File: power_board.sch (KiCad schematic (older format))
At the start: 24 parts

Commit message: Added to the list of parts and started putting parameters on parts in the schematic
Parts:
- removed Q? (x11): Q_NMOS_DGS, symbol Q_NMOS_DGS
- removed Q? (x11): Q_PMOS_DGS, symbol Q_PMOS_DGS
- added D?: LED_CRGB, symbol LED_CRGB
- added R?: R, Resistors_SMD:R_0402, symbol R
- Q?: Continuous Current (none) -> 200mA; Drive Voltage (none) -> 0.9, 4.5V; Manufacturer (none) -> Rohm Semiconductor; Manufacturer PN (none) -> RU1J002YNTCL; Rds on (none) -> 2.2Ohm; Vds (none) -> 50V
- Q?: Continuous Current (none) -> 2.7A; Drive Voltage (none) -> 2.5, 4.5V; Manufacturer (none) -> Diodes Incorporated; Manufacturer PN (none) -> DMP2215L-7; Vds (none) -> 20V
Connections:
- net labels added: +5V, GND, R1, R_Control_1
- wire segments 0 -> 7
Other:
- moved on the sheet: Q?

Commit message: Finished schematics first draft for switching board and found all parts for the board
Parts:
- removed D?: LED_CRGB, symbol LED_CRGB
- added J1: RasPi Conn, symbol Conn_02x20_Odd_Even
- added J2: Power Supply, symbol Conn_01x02_Female
- added J3: MuddPi Conn, symbol Conn_01x20_Female
- added Q10, Q11, Q12, Q17, Q18, Q19, Q2, Q20, Q3, Q4, Q9: Q_NMOS_DGS, symbol Q_NMOS_DGS
- added Q13, Q14, Q15, Q16, Q21, Q22, Q23, Q24, Q6, Q7, Q8: Q_PMOS_DGS, symbol Q_PMOS_DGS
- added R10, R11, R12, R2, R3, R4, R5, R6, R7, R8, R9: 1 kOhm, Resistors_SMD:R_0402, symbol R
- R1: renamed from R?; value R -> 1 kOhm; Resistance 1 kOhm -> (none)
- gave numbers to parts that had none: 2
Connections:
- net labels added: +3.3V, B1, B2, B3, B4, B_Control_1, B_Control_2, B_Control_3, B_Control_4, G1, G2, G3, G4, G_Control_1, G_Control_2, G_Control_3, G_Control_4, MOSI, R_Control_2, R_Control_3, R_Control_4, SCLK, color, isBeat
- wire segments 7 -> 118
- no-connect marks 0 -> 27
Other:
- note added: "1"
- note added: "16 October 2017"
- note added: "A"
- note added: "Hill Balliet"
- note added: "LED Switching\n"

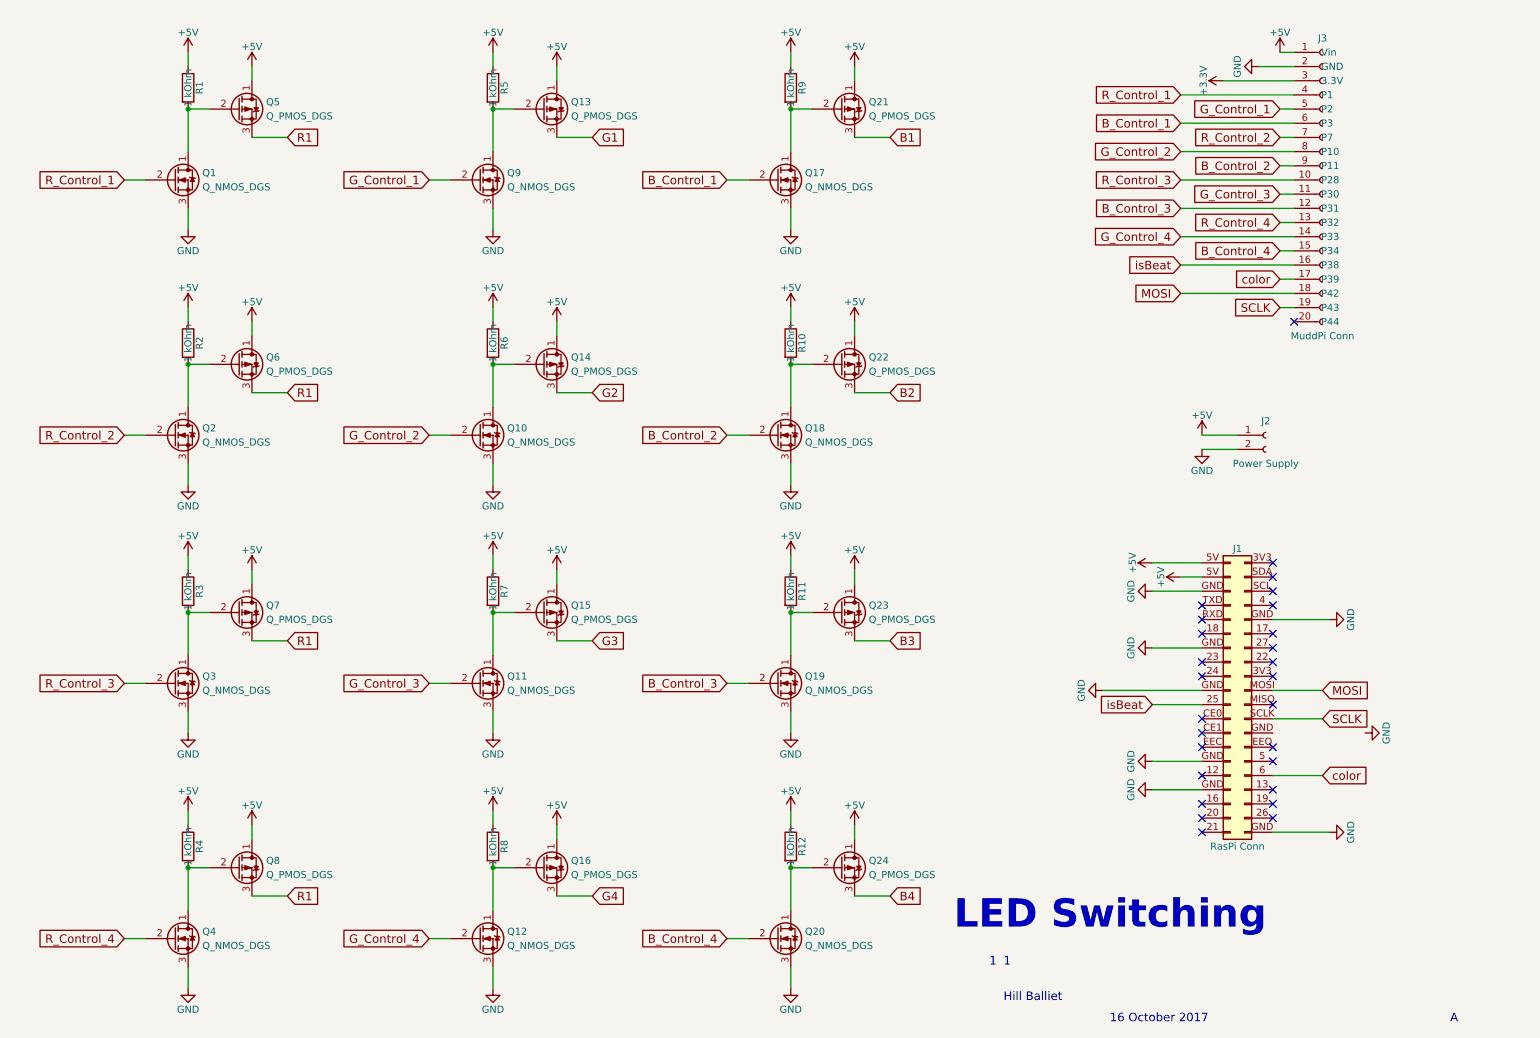
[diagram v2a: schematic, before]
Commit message: Added footprint to the power supply jack.  Fixed a wrong part (raspi connector was 10x2 is now 20x2)
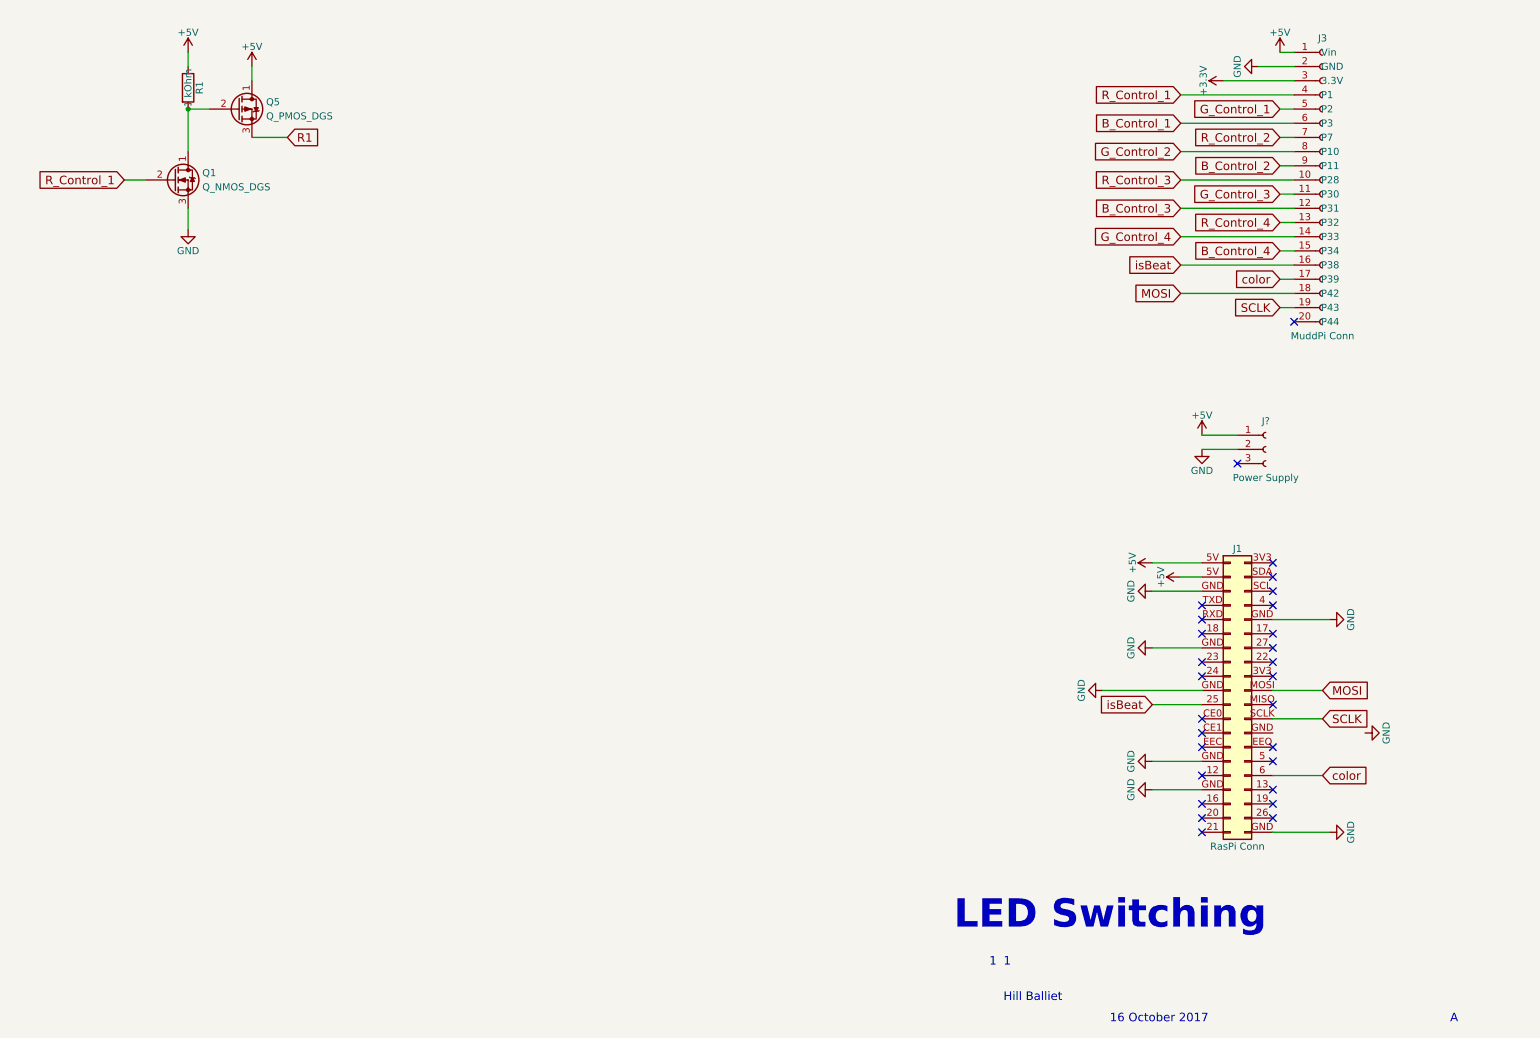
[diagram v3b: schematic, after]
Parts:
- removed J2: Power Supply, symbol Conn_01x02_Female
- removed Q10, Q11, Q12, Q17, Q18, Q19, Q2, Q20, Q3, Q4, Q9: Q_NMOS_DGS, symbol Q_NMOS_DGS
- removed Q13, Q14, Q15, Q16, Q21, Q22, Q23, Q24, Q6, Q7, Q8: Q_PMOS_DGS, symbol Q_PMOS_DGS
- removed R10, R11, R12, R2, R3, R4, R5, R6, R7, R8, R9: 1 kOhm, Resistors_SMD:R_0402, symbol R
- added J?: Power Supply, Connect:BARREL_JACK, symbol Conn_01x03_Female
- Q5: footprint (none) -> TO_SOT_Packages_SMD:SOT-23
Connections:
- net +5V: now also J?.1 (Pin_1)
- net GND: now also J?.2 (Pin_2)
- no-connect marks 27 -> 28

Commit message: Improved schematic symbols and finished making all footprints.  (Need to be checked before finalization)
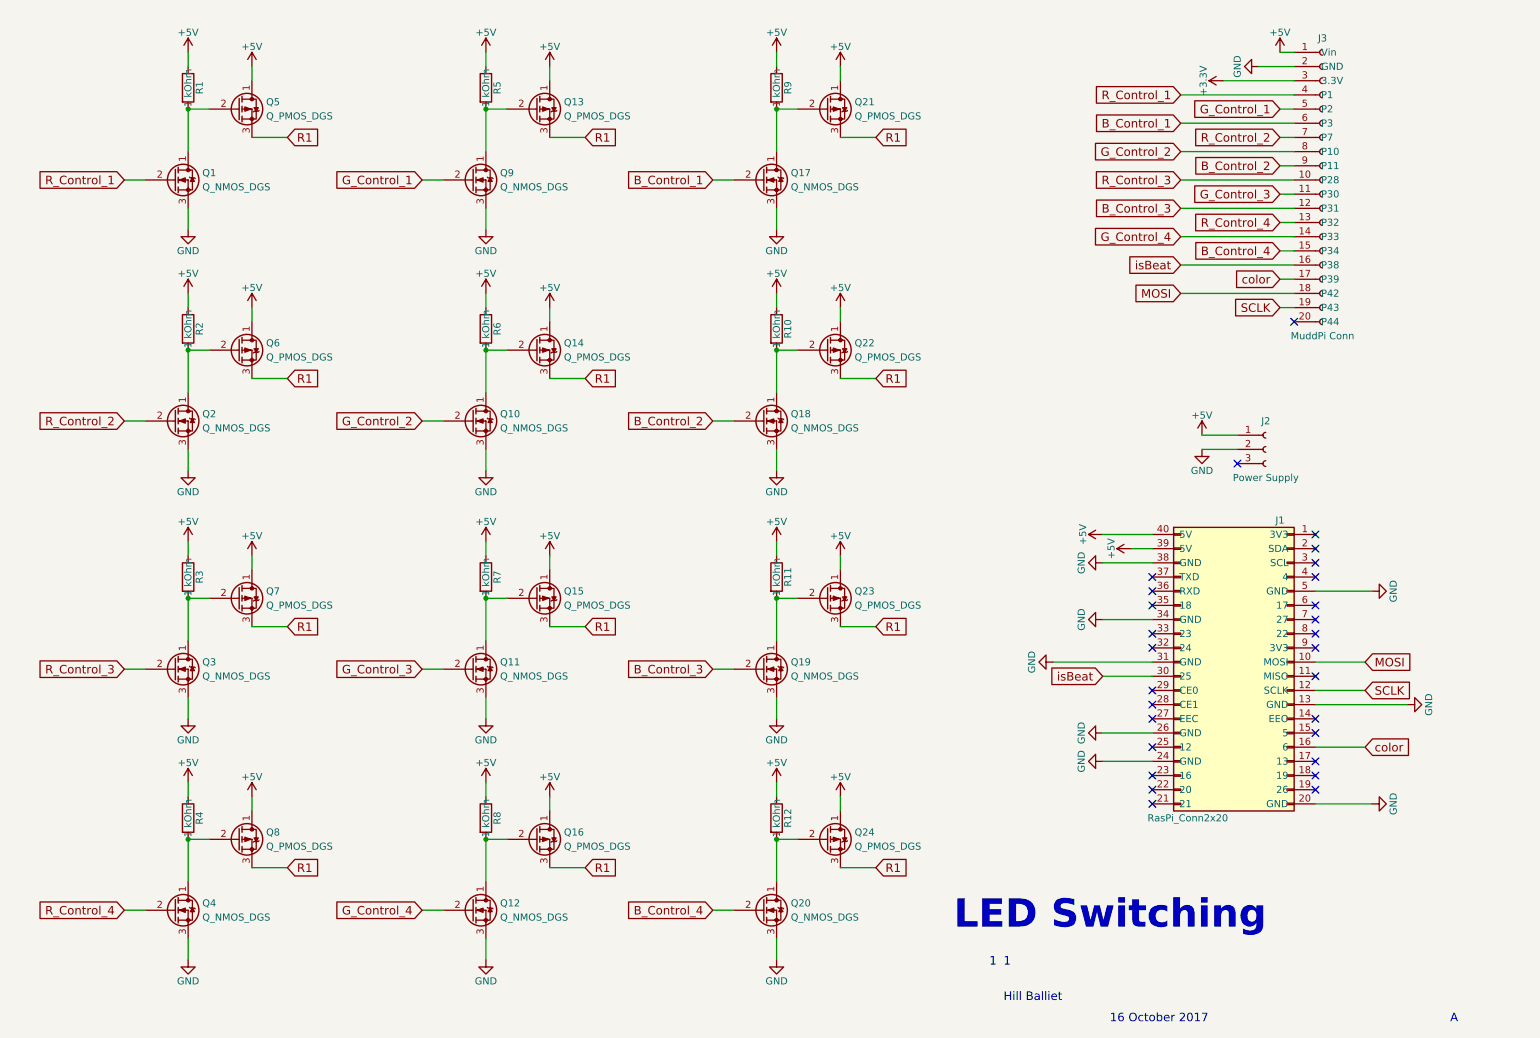
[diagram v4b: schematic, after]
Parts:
- removed J1: RasPi Conn, symbol Conn_02x20_Odd_Even
- added J1: RasPi_Conn2x20, wall:Molex_2x20, symbol RasPi_Conn2x20
- added Q10, Q11, Q12, Q17, Q18, Q19, Q2, Q20, Q3, Q4, Q9: Q_NMOS_DGS, wall:SOT-323FL, symbol Q_NMOS_DGS
- added Q13, Q14, Q15, Q16, Q21, Q22, Q23, Q24, Q6, Q7, Q8: Q_PMOS_DGS, TO_SOT_Packages_SMD:SOT-23, symbol Q_PMOS_DGS
- added R10, R11, R12, R2, R3, R4, R5, R6, R7, R8, R9: 1 kOhm, Resistors_SMD:R_0402, symbol R
- J3: footprint (none) -> wall:Molex_1x20
- Q1: footprint (none) -> wall:SOT-323FL
- gave numbers to parts that had none: 1
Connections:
- net +5V: now also J1.39 (5V), J1.40 (5V), Q13.1 (D), Q14.1 (D), Q15.1 (D), Q16.1 (D), Q21.1 (D), Q22.1 (D), Q23.1 (D), Q24.1 (D), Q6.1 (D), Q7.1 (D), Q8.1 (D), R10.1, R11.1, R12.1, R2.1, R3.1, R4.1, R5.1, R6.1, R7.1, R8.1, R9.1
- net B_Control_1: now also Q17.2 (G)
- net B_Control_2: now also Q18.2 (G)
- net B_Control_3: now also Q19.2 (G)
- net B_Control_4: now also Q20.2 (G)
- net GND: now also J1.13 (GND), J1.20 (GND), J1.24 (GND), J1.26 (GND), J1.31 (GND), J1.34 (GND), J1.38 (GND), J1.5 (GND), Q10.3 (S), Q11.3 (S), Q12.3 (S), Q17.3 (S), Q18.3 (S), Q19.3 (S), Q2.3 (S), Q20.3 (S), Q3.3 (S), Q4.3 (S), Q9.3 (S)
- net G_Control_1: now also Q9.2 (G)
- net G_Control_2: now also Q10.2 (G)
- net G_Control_3: now also Q11.2 (G)
- net G_Control_4: now also Q12.2 (G)
- net MOSI: now also J1.10 (MOSI)
- net R1: now also Q13.3 (S), Q14.3 (S), Q15.3 (S), Q16.3 (S), Q21.3 (S), Q22.3 (S), Q23.3 (S), Q24.3 (S), Q6.3 (S), Q7.3 (S), Q8.3 (S)
- net R_Control_2: now also Q2.2 (G)
- net R_Control_3: now also Q3.2 (G)
- net R_Control_4: now also Q4.2 (G)
- net SCLK: now also J1.12 (SCLK)
- net color: now also J1.16 (6)
- net isBeat: now also J1.30 (25)
- new net: Q2.1 (D), Q6.2 (G), R2.2
- new net: Q3.1 (D), Q7.2 (G), R3.2
- new net: Q4.1 (D), Q8.2 (G), R4.2
- new net: Q13.2 (G), Q9.1 (D), R5.2
- new net: Q10.1 (D), Q14.2 (G), R6.2
- new net: Q11.1 (D), Q15.2 (G), R7.2
- new net: Q12.1 (D), Q16.2 (G), R8.2
- new net: Q17.1 (D), Q21.2 (G), R9.2
- new net: Q18.1 (D), Q22.2 (G), R10.2
- new net: Q19.1 (D), Q23.2 (G), R11.2
- new net: Q20.1 (D), Q24.2 (G), R12.2

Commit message: Added info for best board manufacturer and fixed issues with connections on the schematic.  Checked pinouts
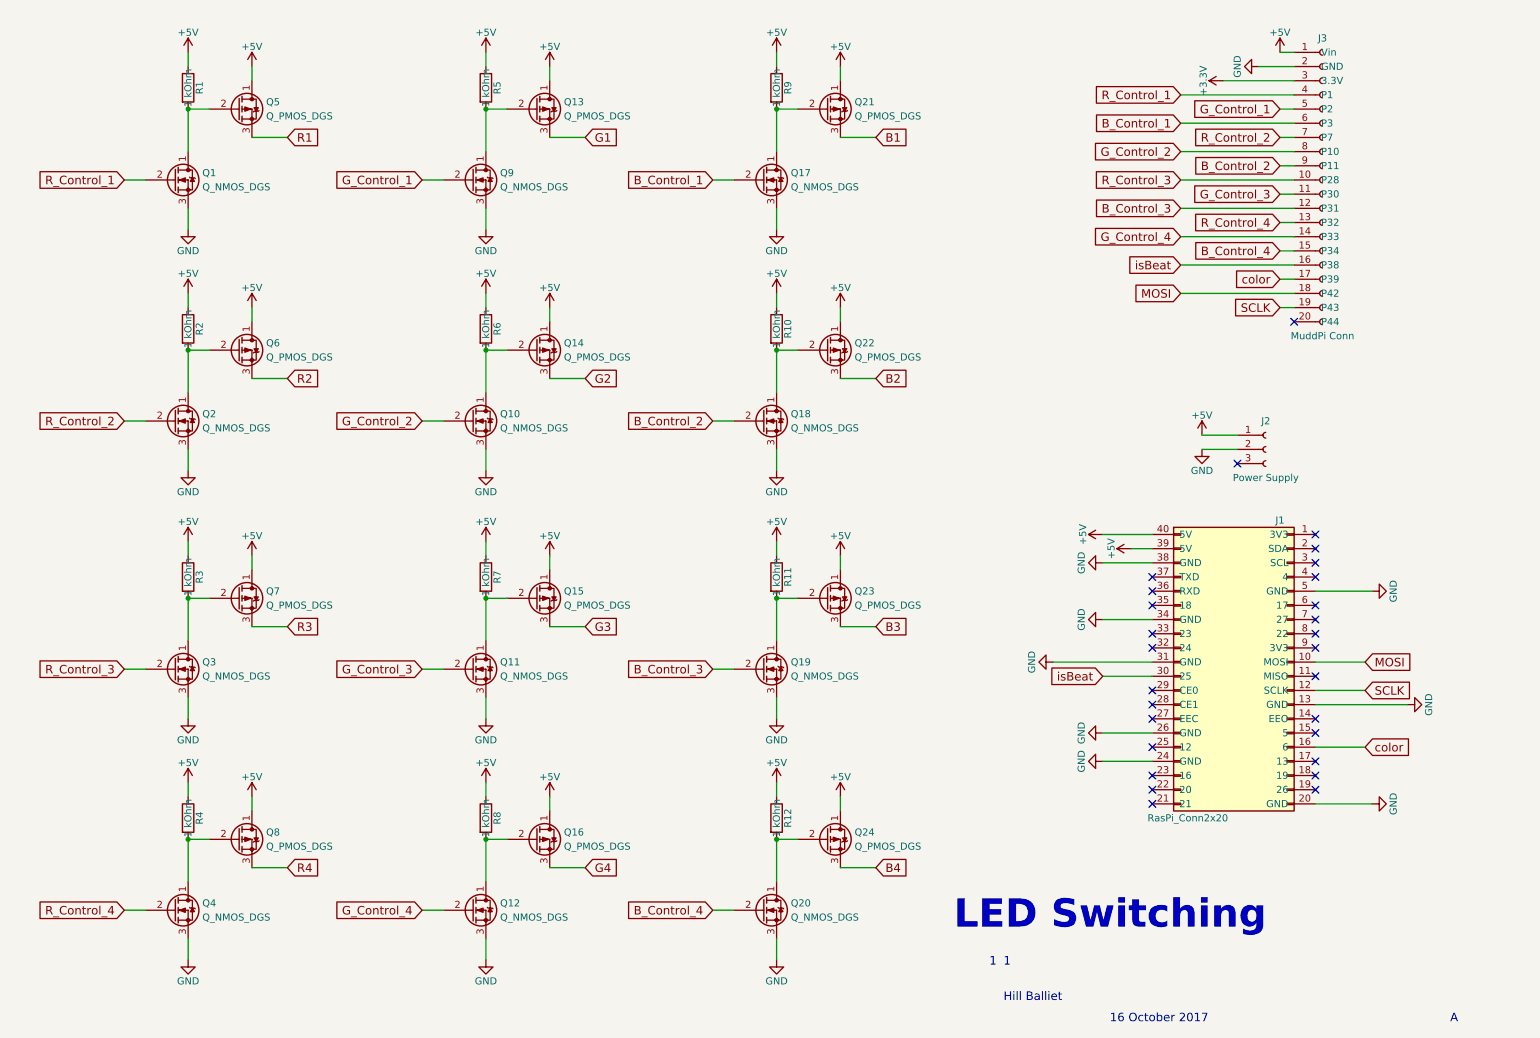
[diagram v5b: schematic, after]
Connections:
- net R1: no longer Q13.3 (S), Q14.3 (S), Q15.3 (S), Q16.3 (S), Q21.3 (S), Q22.3 (S), Q23.3 (S), Q24.3 (S), Q6.3 (S), Q7.3 (S), Q8.3 (S)
- new net B1: Q21.3 (S)
- new net B2: Q22.3 (S)
- new net B3: Q23.3 (S)
- new net B4: Q24.3 (S)
- new net G1: Q13.3 (S)
- new net G2: Q14.3 (S)
- new net G3: Q15.3 (S)
- new net G4: Q16.3 (S)
- new net R2: Q6.3 (S)
- new net R3: Q7.3 (S)
- new net R4: Q8.3 (S)
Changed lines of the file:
@@
 $EndComp
 Text GLabel 2350 3100 2    60   Input ~ 0
-R1
+R2
 Connection ~ 1650 2900
 Wire Wire Line
@@
 $EndComp
 Text GLabel 2350 4850 2    60   Input ~ 0
-R1
+R3
 Connection ~ 1650 4650
 Wire Wire Line
@@
 $EndComp
 Text GLabel 2350 6550 2    60   Input ~ 0
-R1
+R4
 Connection ~ 1650 6350
 Wire Wire Line
@@
 $EndComp
 Text GLabel 4450 1400 2    60   Input ~ 0
-R1
+G1
 Connection ~ 3750 1200
 Wire Wire Line
@@
 $EndComp
 Text GLabel 4450 3100 2    60   Input ~ 0
-R1
+G2
 Connection ~ 3750 2900
 Wire Wire Line
@@
 $EndComp
 Text GLabel 4450 4850 2    60   Input ~ 0
-R1
+G3
 Connection ~ 3750 4650
 Wire Wire Line
@@
 $EndComp
 Text GLabel 4450 6550 2    60   Input ~ 0
-R1
+G4
 Connection ~ 3750 6350
 Wire Wire Line
@@
 $EndComp
 Text GLabel 6500 1400 2    60   Input ~ 0
-R1
+B1
 Connection ~ 5800 1200
 Wire Wire Line
@@
 $EndComp
 Text GLabel 6500 3100 2    60   Input ~ 0
-R1
+B2
 Connection ~ 5800 2900
 Wire Wire Line
@@
 $EndComp
 Text GLabel 6500 4850 2    60   Input ~ 0
-R1
+B3
 Connection ~ 5800 4650
 Wire Wire Line
@@
 $EndComp
 Text GLabel 6500 6550 2    60   Input ~ 0
-R1
+B4
 Connection ~ 5800 6350
 Wire Wire Line
